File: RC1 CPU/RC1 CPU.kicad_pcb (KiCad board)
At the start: 2 copper layers, 99.1 x 99.1 mm, 7 parts, among them J1 Expansion, J2 RC1_UI_Port, J3 BARREL_JACK, M1 Mounting, M2 Mounting, M3 Mounting, M4 Mounting

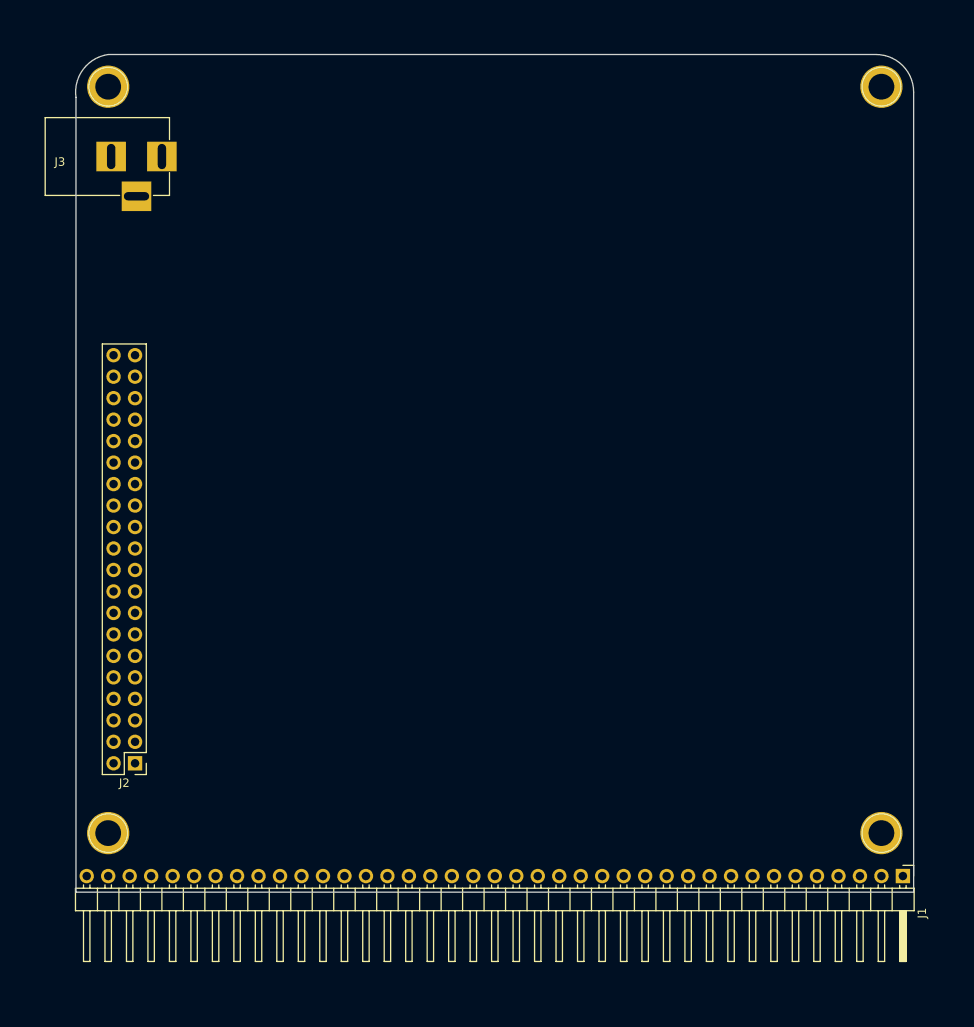
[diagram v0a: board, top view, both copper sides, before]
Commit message: Routed most signals on CPU board
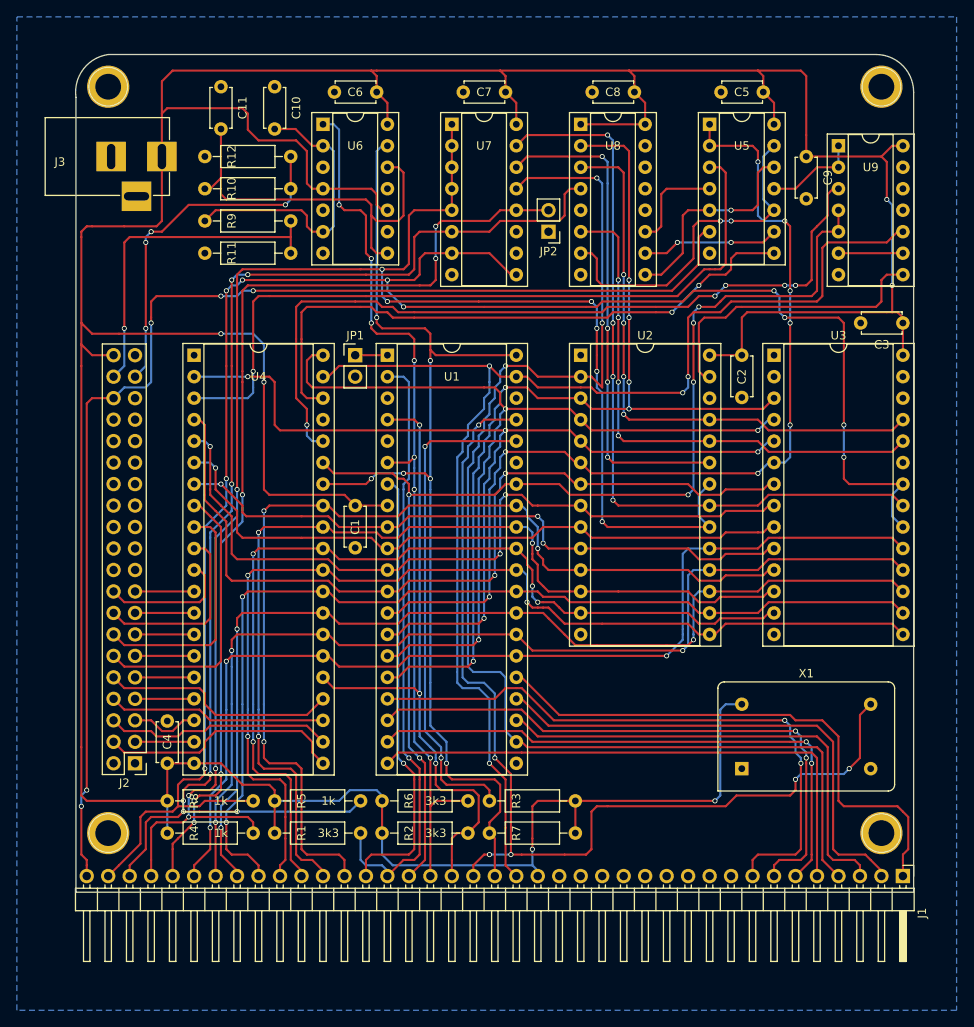
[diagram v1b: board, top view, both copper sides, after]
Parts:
- added C1: 100nF, Capacitors_THT:C_Disc_D4.7mm_W2.5mm_P5.00mm, F.Cu at (133.3, 101.6)
- added C10: 220nF, Capacitors_THT:C_Disc_D4.7mm_W2.5mm_P5.00mm, F.Cu at (123.8, 52.1)
- added C11: 220nF, Capacitors_THT:C_Disc_D4.7mm_W2.5mm_P5.00mm, F.Cu at (117.5, 52.1)
- added C2: 100nF, Capacitors_THT:C_Disc_D4.7mm_W2.5mm_P5.00mm, F.Cu at (179.1, 83.8)
- added C3: 100nF, Capacitors_THT:C_Disc_D4.7mm_W2.5mm_P5.00mm, F.Cu at (198.1, 80.0)
- added C4: 100nF, Capacitors_THT:C_Disc_D4.7mm_W2.5mm_P5.00mm, F.Cu at (111.1, 132.1)
- added C5: 100nF, Capacitors_THT:C_Disc_D4.7mm_W2.5mm_P5.00mm, F.Cu at (181.6, 52.7)
- added C6: 100nF, Capacitors_THT:C_Disc_D4.7mm_W2.5mm_P5.00mm, F.Cu at (135.9, 52.7)
- added C7: 100nF, Capacitors_THT:C_Disc_D4.7mm_W2.5mm_P5.00mm, F.Cu at (151.1, 52.7)
- added C8: 100nF, Capacitors_THT:C_Disc_D4.7mm_W2.5mm_P5.00mm, F.Cu at (166.4, 52.7)
- added C9: 100nF, Capacitors_THT:C_Disc_D4.7mm_W2.5mm_P5.00mm, F.Cu at (186.7, 60.3)
- added JP1: VP_GND, Pin_Headers:Pin_Header_Straight_1x02_Pitch2.54mm, F.Cu at (133.3, 83.8)
- added JP2: DEN, Pin_Headers:Pin_Header_Straight_1x02_Pitch2.54mm, F.Cu at (156.2, 69.2)
- added R1: 3k3, Resistors_THT:R_Axial_DIN0207_L6.3mm_D2.5mm_P10.16mm_Horizontal, F.Cu at (134.0, 140.3)
- added R10: 1k, Resistors_THT:R_Axial_DIN0207_L6.3mm_D2.5mm_P10.16mm_Horizontal, F.Cu at (115.6, 64.1)
- added R11: 47k, Resistors_THT:R_Axial_DIN0207_L6.3mm_D2.5mm_P10.16mm_Horizontal, F.Cu at (115.6, 71.8)
- added R12: 47k, Resistors_THT:R_Axial_DIN0207_L6.3mm_D2.5mm_P10.16mm_Horizontal, F.Cu at (115.6, 60.3)
- added R2: 3k3, Resistors_THT:R_Axial_DIN0207_L6.3mm_D2.5mm_P10.16mm_Horizontal, F.Cu at (146.7, 140.3)
- added R3: 3.3k, Resistors_THT:R_Axial_DIN0207_L6.3mm_D2.5mm_P10.16mm_Horizontal, F.Cu at (149.2, 136.5)
- added R4: 1k, Resistors_THT:R_Axial_DIN0207_L6.3mm_D2.5mm_P10.16mm_Horizontal, F.Cu at (111.1, 140.3)
- added R5: 1k, Resistors_THT:R_Axial_DIN0207_L6.3mm_D2.5mm_P10.16mm_Horizontal, F.Cu at (123.8, 136.5)
- added R6: 3k3, Resistors_THT:R_Axial_DIN0207_L6.3mm_D2.5mm_P10.16mm_Horizontal, F.Cu at (146.7, 136.5)
- added R7: 3k3, Resistors_THT:R_Axial_DIN0207_L6.3mm_D2.5mm_P10.16mm_Horizontal, F.Cu at (149.2, 140.3)
- added R8: 1k, Resistors_THT:R_Axial_DIN0207_L6.3mm_D2.5mm_P10.16mm_Horizontal, F.Cu at (111.1, 136.5)
- added R9: 1k, Resistors_THT:R_Axial_DIN0207_L6.3mm_D2.5mm_P10.16mm_Horizontal, F.Cu at (115.6, 67.9)
- added U1: WD65C02, Housings_DIP:DIP-40_W15.24mm_Socket, F.Cu at (137.2, 83.8)
- added U2: HM62256BLP-7, Housings_DIP:DIP-28_W15.24mm_Socket, F.Cu at (160.0, 83.8)
- added U3: 28C256, Housings_DIP:DIP-28_W15.24mm_Socket, F.Cu at (182.9, 83.8)
- added U4: 6532, Housings_DIP:DIP-40_W15.24mm_Socket, F.Cu at (114.3, 83.8)
- added U5: 74LS00, Housings_DIP:DIP-14_W7.62mm_Socket, F.Cu at (175.3, 56.5)
- added U6: LM556, Housings_DIP:DIP-14_W7.62mm_Socket, F.Cu at (129.5, 56.5)
- added U7: 74LS145, Housings_DIP:DIP-16_W7.62mm_Socket, F.Cu at (144.8, 56.5)
- added U8: 74LS138, Housings_DIP:DIP-16_W7.62mm_Socket, F.Cu at (160.0, 56.5)
- added U9: 74LS00, Housings_DIP:DIP-14_W7.62mm_Socket, F.Cu at (190.5, 59.1)
- added X1: 1MHz, Oscillators:Oscillator_DIP-14, F.Cu at (179.1, 132.7)
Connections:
- J1 pad 1: (no net) -> /A15
- J1 pad 10: (no net) -> /A6
- J1 pad 11: (no net) -> /A5
- J1 pad 12: (no net) -> /A4
- J1 pad 13: (no net) -> /A3
- J1 pad 14: (no net) -> /A2
- J1 pad 15: (no net) -> /A1
- J1 pad 16: (no net) -> /A0
- J1 pad 19: (no net) -> /PHI2
- J1 pad 2: (no net) -> /A14
- J1 pad 20: (no net) -> /~RESET
- J1 pad 21: (no net) -> /PHI0
- J1 pad 22: (no net) -> /~IRQ
- J1 pad 23: (no net) -> /~NMI
- J1 pad 24: (no net) -> /R/~W
- J1 pad 25: (no net) -> /~RDY
- J1 pad 26: (no net) -> /SYNC
- J1 pad 27: (no net) -> /D0
- J1 pad 28: (no net) -> /D1
- J1 pad 29: (no net) -> /D2
- J1 pad 3: (no net) -> /A13
- J1 pad 30: (no net) -> /D3
- J1 pad 31: (no net) -> /D4
- J1 pad 32: (no net) -> /D5
- J1 pad 33: (no net) -> /D6
- J1 pad 34: (no net) -> /D7
- J1 pad 35: (no net) -> /DEN
- J1 pad 36: (no net) -> K0
- J1 pad 37: (no net) -> K5
- J1 pad 38: (no net) -> K7
- J1 pad 39: (no net) -> IO3
- J1 pad 4: (no net) -> /A12
- J1 pad 5: (no net) -> /A11
- J1 pad 6: (no net) -> /A10
- J1 pad 7: (no net) -> /A9
- J1 pad 8: (no net) -> /A8
- J1 pad 9: (no net) -> /A7
- J2 pad 1: (no net) -> GND
- J2 pad 10: (no net) -> /PB0
- J2 pad 11: (no net) -> /PA7
- J2 pad 12: (no net) -> /PA0
- J2 pad 13: (no net) -> /PA6
- J2 pad 14: (no net) -> /PA1
- J2 pad 15: (no net) -> /PA5
- J2 pad 16: (no net) -> /PA2
- J2 pad 17: (no net) -> /PA4
- J2 pad 18: (no net) -> /PA3
- J2 pad 2: VCC -> GND
- J2 pad 3: (no net) -> /PB4
- J2 pad 36: (no net) -> IO3
- J2 pad 37: (no net) -> RS
- J2 pad 38: (no net) -> ST
- J2 pad 39: (no net) -> GND
- J2 pad 4: (no net) -> /PB3
- J2 pad 40: (no net) -> VCC
- J2 pad 5: (no net) -> /PB5
- J2 pad 6: (no net) -> /PB2
- J2 pad 7: (no net) -> /PB6
- J2 pad 8: (no net) -> /PB1
- J2 pad 9: (no net) -> /PB7
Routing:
- net VCC: track 0.00 -> 499.2 mm, vias 0 -> 6
- net K7: track 0.00 -> 218.6 mm, vias 0 -> 10
- net K0: track 0.00 -> 203.4 mm, vias 0 -> 10
- net /A10: track 0.00 -> 158.5 mm, vias 0 -> 6
- net /PHI2: track 0.00 -> 152.4 mm, vias 0 -> 4
- net /A12: track 0.00 -> 150.2 mm, vias 0 -> 3
- net K5: track 0.00 -> 149.4 mm, vias 0 -> 7
- net IO3: track 0.00 -> 145.9 mm, vias 0 -> 5
- net /R/~W: track 0.00 -> 143.1 mm, vias 0 -> 6
- net /A8: track 0.00 -> 141.5 mm, vias 0 -> 6
- net /A9: track 0.00 -> 133.7 mm, vias 0 -> 6
- net /A11: track 0.00 -> 124.4 mm, vias 0 -> 4
- net /D3: track 0.00 -> 124.4 mm, vias 0 -> 3
- net /~RESET: track 0.00 -> 124.0 mm, vias 0 -> 6
- net /PHI0: track 0.00 -> 122.3 mm, vias 0 -> 6
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- added copper zone on B.Cu, net GND

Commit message: Added UI signals to CPU board
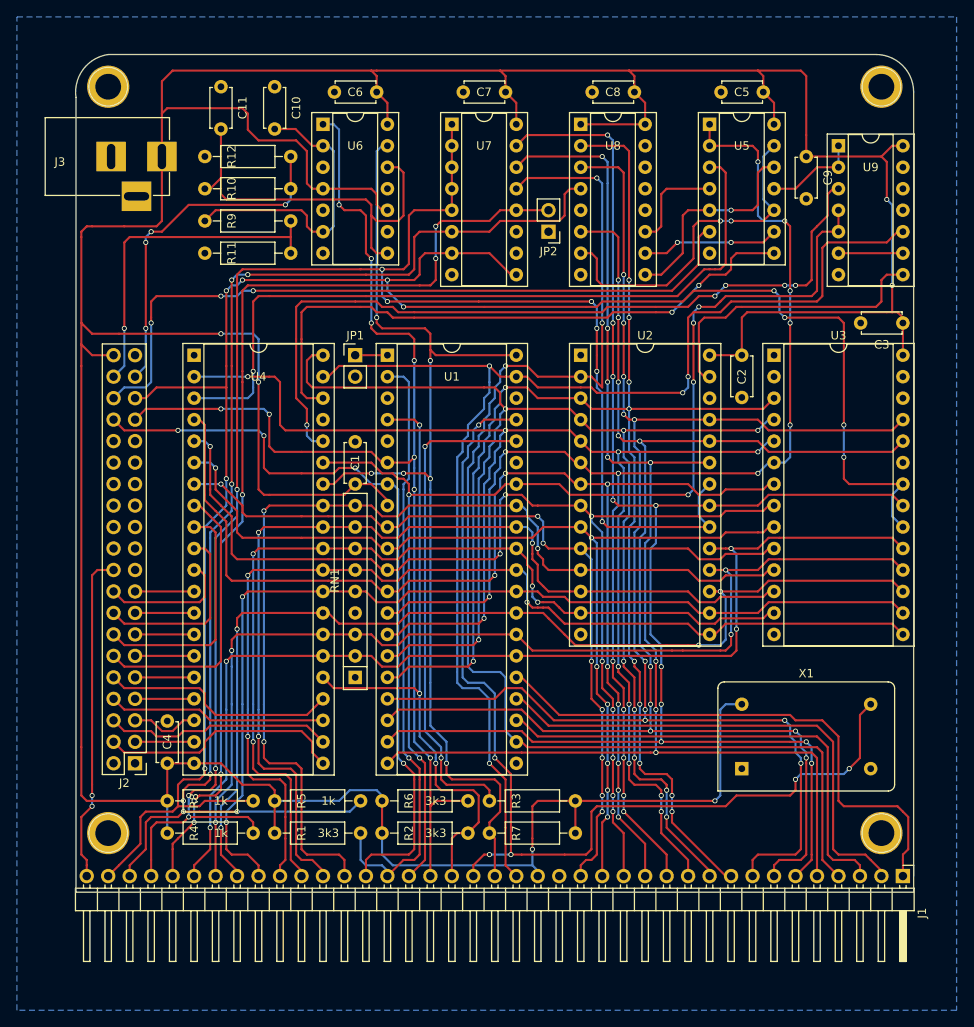
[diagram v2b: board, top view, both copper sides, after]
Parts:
- added RN1: 4k7x8, Resistors_THT:R_Array_SIP9, F.Cu at (133.3, 121.9)
- moved C1 2.54 mm to (133.3, 99.1), turned to 90 degrees
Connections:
- J1 pad 39: IO3 -> TAPE
- J2 pad 20: (no net) -> TAPE
- J2 pad 33: (no net) -> /~NMI
- J2 pad 34: (no net) -> /SYNC
- J2 pad 35: (no net) -> K7
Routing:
- net /A7: track 114.7 -> 177.3 mm, vias 6 -> 11
- net IO3: track 145.9 -> 86.1 mm, vias 5 -> 3
- net /A6: track 103.8 -> 162.7 mm, vias 3 -> 9
- net /A5: track 111.3 -> 166.9 mm, vias 4 -> 10
- net /A4: track 114.1 -> 164.6 mm, vias 8 -> 14
- net /A3: track 99.6 -> 147.8 mm, vias 2 -> 8
- net /A2: track 90.5 -> 134.6 mm, vias 3 -> 9
- net /A0: track 75.8 -> 117.0 mm, vias 3 -> 8
- net /A1: track 77.9 -> 118.9 mm, vias 1 -> 7
- net TAPE: track 0.00 -> 39.2 mm, vias 0 -> 2
- net /SYNC: track 53.0 -> 91.3 mm, vias 1 -> 4
- net /A8: track 141.5 -> 178.1 mm, vias 6 -> 10
- net /A9: track 133.7 -> 169.1 mm, vias 6 -> 10
- net /~NMI: track 106.4 -> 141.6 mm, vias 7 -> 9
- net /A11: track 124.4 -> 159.5 mm, vias 4 -> 8
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
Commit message: Added phi1 to UI connector
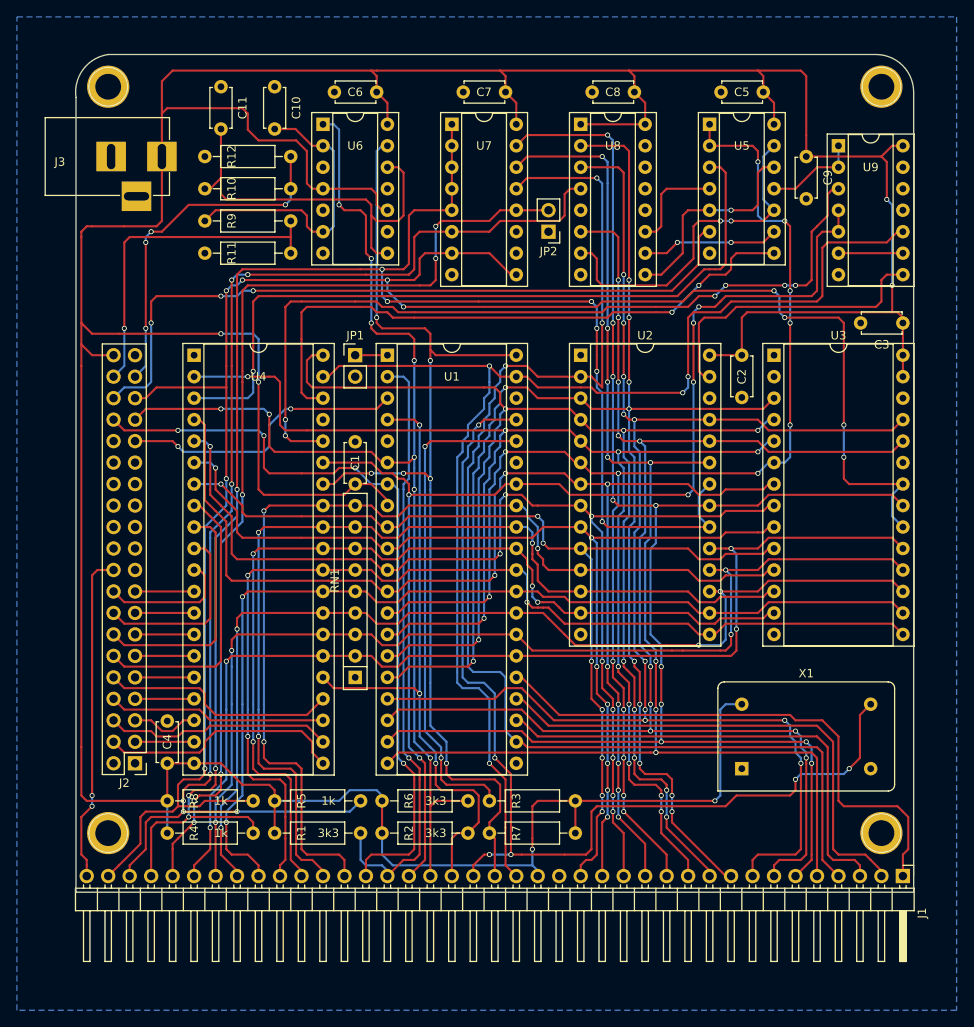
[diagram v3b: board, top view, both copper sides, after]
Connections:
- J2 pad 31: (no net) -> /PHI1
- U1 pad 3: (no net) -> /PHI1
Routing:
- net /PHI1: track 0.00 -> 34.5 mm, vias 0 -> 2
- net RAM_SEL: track 93.7 -> 97.0 mm, vias 5 -> 6
- net VCC: track 501.0 -> 503.6 mm
- net /D5: track 123.5 -> 124.2 mm
